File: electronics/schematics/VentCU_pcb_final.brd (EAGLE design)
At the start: 51.1 x 22.9 mm, 12 parts, among them U1 ADS1115IDGST, X1 TERMINAL-BLOCK-3.5MM-6-PIN-RO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, X2 TERMINAL-BLOCK-3.5MM-4-PIN-RO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

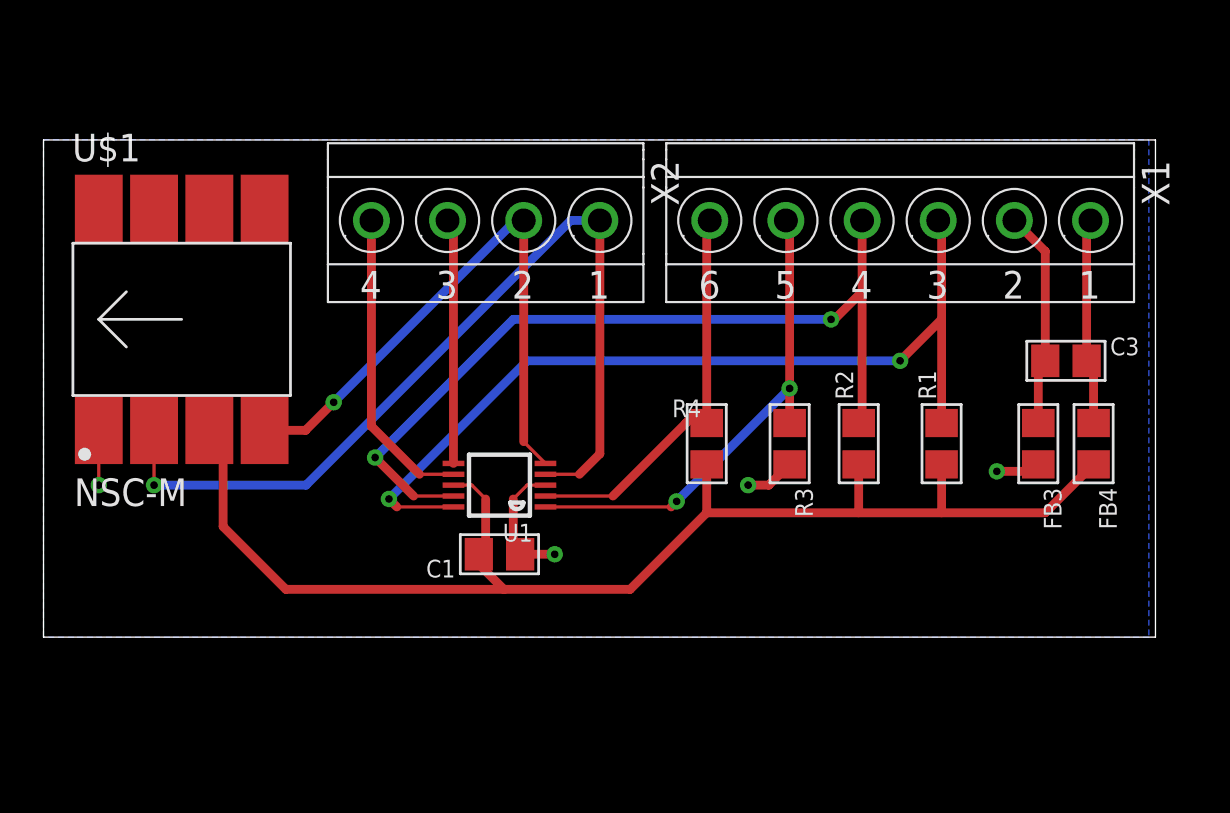
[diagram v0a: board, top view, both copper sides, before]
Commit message: Updated design for better signal integrity, size
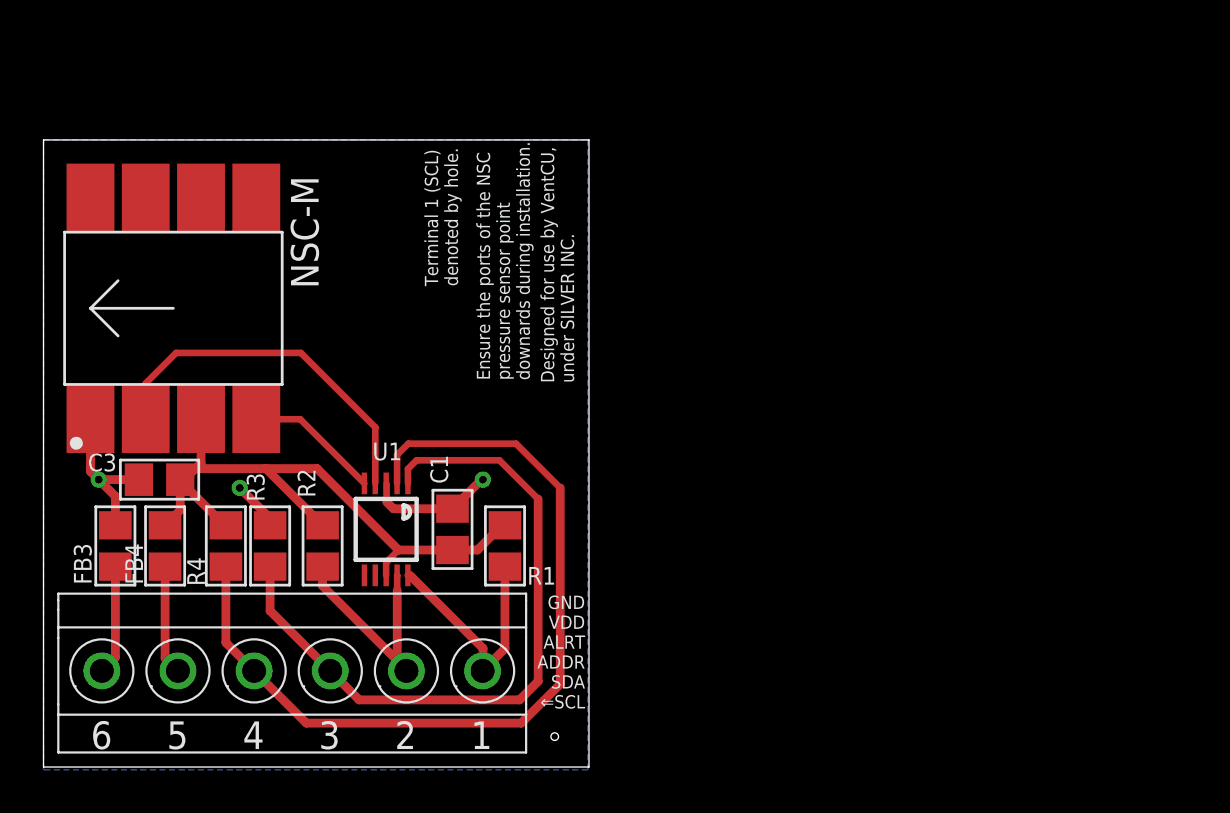
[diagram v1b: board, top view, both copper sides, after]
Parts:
- removed X2: TERMINAL-BLOCK-3.5MM-4-PIN-ROUND-PAD, Rembrandt Electronics - Terminal Block 3-5mm v1-0:TERMINAL-BLOCK-4-PIN-3.5MM-ROUND-PAD
- moved FB4 42.9 mm to (5.59, 61.3)
- moved FB3 42.7 mm to (3.30, 61.3)
- moved C3 42.0 mm to (5.33, 64.4)
- moved X1 34.8 mm to (11.4, 55.5)
- moved R2 25.1 mm to (12.8, 61.3), turned to 270 degrees
- moved R3 24.3 mm to (10.4, 61.3), turned to 90 degrees
- moved R4 22.6 mm to (8.38, 61.3), turned to 270 degrees
- moved R1 20.6 mm to (21.2, 61.3), turned to 270 degrees
- moved U1 5.59 mm to (15.7, 62.1), turned to 180 degrees
- moved C1 2.44 mm to (18.8, 62.1), turned to 270 degrees
- moved U$1 0.64 mm to (5.97, 72.3)
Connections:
- net ADDR: now also X1.3; no longer X1.5
- net AIN0: no longer X2.1
- net AIN1: no longer X2.2
- net AIN2: no longer X2.3
- net AIN3: no longer X2.4
- net ALERT: now also X1.4; no longer X1.6
- net GND: now also C3.1, FB3.1; no longer FB3.2
- net N$1: now also FB4.2, X1.5; no longer C3.2, FB4.1, X1.1
- net N$2: now also FB3.2, X1.6; no longer C3.1, FB3.1, X1.2
- net SCL: now also X1.1; no longer X1.3
- net SDA: now also X1.2; no longer X1.4
- net VDD: now also C3.2, FB4.1; no longer FB4.2
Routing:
- net VDD: track 61.4 -> 30.0 mm
- net SCL: track 41.3 -> 11.1 mm, vias 2 -> 0
- net SDA: track 39.2 -> 11.0 mm, vias 2 -> 0
- net AIN0: track 41.7 -> 16.8 mm, vias 1 -> 0
- net AIN1: track 27.5 -> 6.19 mm, vias 1 -> 0
- net ALERT: track 19.3 -> 40.0 mm
- net AIN3: track 14.1 -> 0.00 mm
- net AIN2: track 11.3 -> 0.00 mm
- net ADDR: track 22.9 -> 32.3 mm, vias 2 -> 0
- net N$2: track 10.0 -> 5.05 mm
- net N$1: track 9.52 -> 5.04 mm
- net GND: track 12.9 -> 15.5 mm, vias 4 -> 3
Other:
- board size 51.1 x 22.9 mm -> 25.1 x 28.8 mm
- board text added: "Designed for use by VentCU, under SILVER INC."
- board text added: "Ensure the ports of the NSC pressure sensor point downards during installation."
- board text added: "GND VDD ALRT ADDR SDA ⇐SCL"
- board text added: "Read the VentCU User Manual before using this PCB. Improper handling can cause failure during operation."
- board text added: "Terminal 1 (SCL) denoted by hole."
